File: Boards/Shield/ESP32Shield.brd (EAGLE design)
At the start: 58.4 x 25.4 mm, 26 parts, among them Q1 220mA/50V/3.5Ω, U1 5V

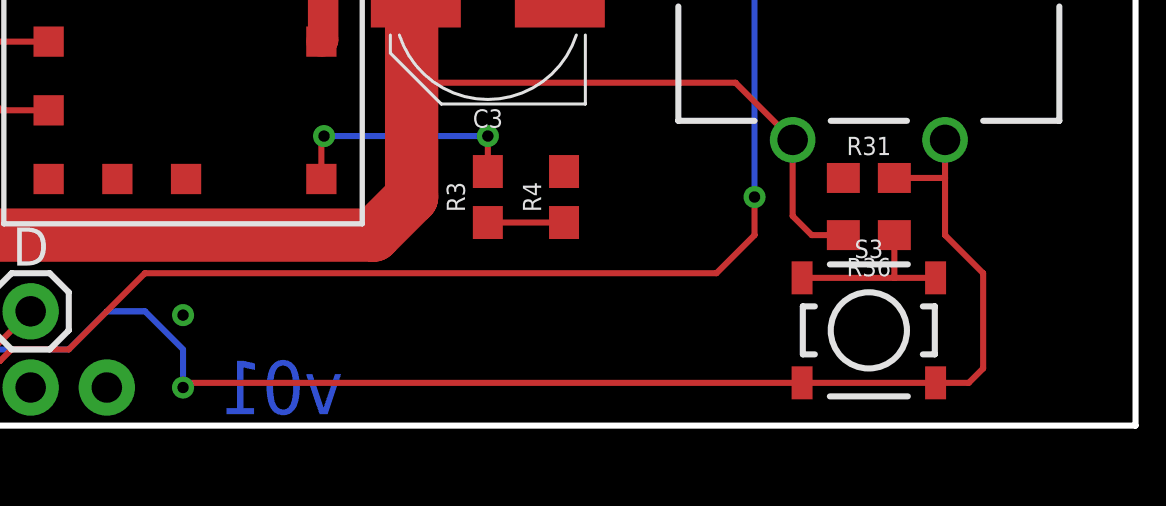
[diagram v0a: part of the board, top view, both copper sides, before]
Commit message: adding new pushbutton
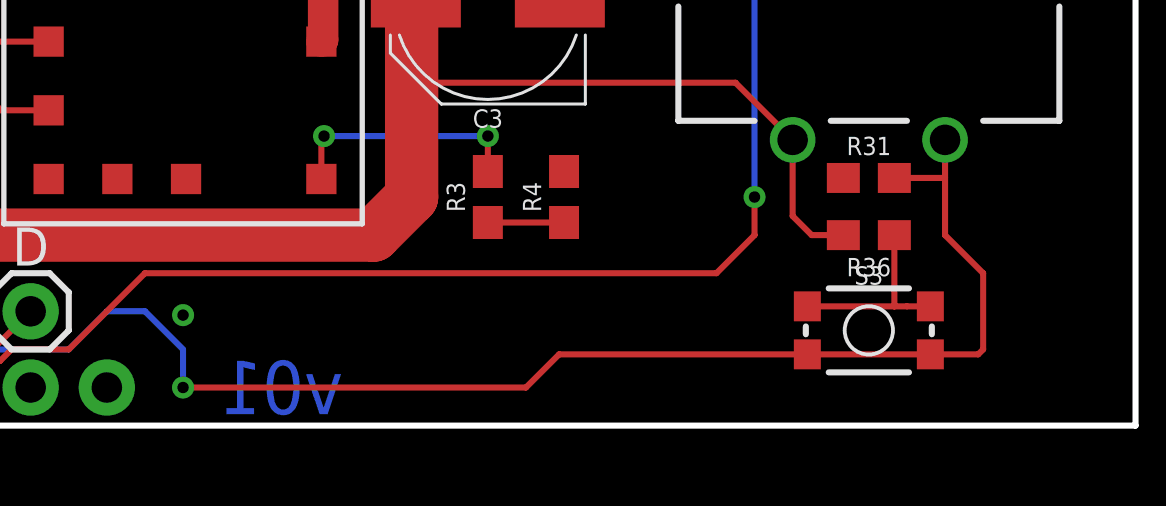
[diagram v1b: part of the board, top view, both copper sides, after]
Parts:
- S3: value MOMENTARY-SWITCH-SPST-SMD-4.5MM -> MOMENTARY-SWITCH-SPST-SMD-4.6X2.8MM; device SparkFun-Switches:TACTILE_SWITCH_SMD_4.5MM -> SparkFun-Switches:TACTILE_SWITCH_SMD_4.6X2.8MM
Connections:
- net BTN: now also S3.1; no longer S3.3
- net N$17: now also S3.3; no longer S3.1
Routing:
- net N$17: track 5.88 -> 6.48 mm
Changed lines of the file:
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@@
 <attribute name="SF_SKU" value="COM-09117" x="49.53" y="13.97" size="1.778" layer="27" rot="R90" display="off"/>
 </element>
-<element name="S3" library="SparkFun-Switches" package="TACTILE_SWITCH_SMD_4.5MM" value="MOMENTARY-SWITCH-SPST-SMD-4.5MM" x="49.53" y="0.635">
-<attribute name="PROD_ID" value="SWCH-09213" x="49.53" y="0.635" size="1.778" layer="27" display="off"/>
+<element name="S3" library="SparkFun-Switches" package="TACTILE_SWITCH_SMD_4.6X2.8MM" value="MOMENTARY-SWITCH-SPST-SMD-4.6X2.8MM" x="49.53" y="0.635">
+<attribute name="PROD_ID" value="SWCH-13065" x="49.53" y="0.635" size="1.778" layer="27" display="off"/>
 </element>
 <element name="U$2" library="SparkFun-IC-Power" package="DC-DC_CONVERTER" value="DC-DC_CONVERTER" x="26.67" y="10.16"/>
@@
 <contactref element="R31" pad="2"/>
 <contactref element="S3" pad="2"/>
-<contactref element="S3" pad="3"/>
+<contactref element="S3" pad="1"/>
 <contactref element="S1" pad="SW-"/>
 <wire x1="52.07" y1="6.985" x2="52.07" y2="5.715" width="0.2032" layer="1"/>
 <wire x1="52.07" y1="5.715" x2="52.07" y2="3.81" width="0.2032" layer="1"/>
 <wire x1="52.07" y1="3.81" x2="53.34" y2="2.54" width="0.2032" layer="1"/>
-<wire x1="53.34" y1="2.54" x2="53.34" y2="-0.635" width="0.2032" layer="1"/>
-<wire x1="53.34" y1="-0.635" x2="52.86" y2="-1.115" width="0.2032" layer="1"/>
-<wire x1="52.86" y1="-1.115" x2="51.755" y2="-1.115" width="0.2032" layer="1"/>
-<wire x1="51.755" y1="-1.115" x2="47.305" y2="-1.115" width="0.2032" layer="1"/>
+<wire x1="51.58" y1="-0.165" x2="47.48" y2="-0.165" width="0.2032" layer="1"/>
 <wire x1="50.38" y1="5.715" x2="52.07" y2="5.715" width="0.2032" layer="1"/>
 <via x="26.67" y="-1.27" extent="1-16" drill="0.381"/>
@@
 <wire x1="22.86" y1="0" x2="5.08" y2="0" width="0.2032" layer="16"/>
 <wire x1="26.67" y1="-1.27" x2="26.825" y2="-1.115" width="0.2032" layer="1"/>
-<wire x1="26.825" y1="-1.115" x2="47.305" y2="-1.115" width="0.2032" layer="1"/>
 <contactref element="J6" pad="2"/>
 <wire x1="3.81" y1="-1.27" x2="5.08" y2="0" width="0.2032" layer="16"/>
+<wire x1="53.34" y1="2.54" x2="53.34" y2="0" width="0.2032" layer="1"/>
+<wire x1="53.34" y1="0" x2="53.175" y2="-0.165" width="0.2032" layer="1"/>
+<wire x1="53.175" y1="-0.165" x2="51.58" y2="-0.165" width="0.2032" layer="1"/>
+<wire x1="47.48" y1="-0.165" x2="39.205" y2="-0.165" width="0.2032" layer="1"/>
+<wire x1="39.205" y1="-0.165" x2="38.1" y2="-1.27" width="0.2032" layer="1"/>
+<wire x1="38.1" y1="-1.27" x2="26.67" y2="-1.27" width="0.2032" layer="1"/>
 </signal>
 <signal name="N$17">
 <contactref element="R36" pad="1"/>
-<contactref element="S3" pad="1"/>
+<contactref element="S3" pad="3"/>
 <contactref element="S3" pad="4"/>
-<wire x1="51.755" y1="2.385" x2="50.38" y2="2.385" width="0.2032" layer="1"/>
-<wire x1="50.38" y1="2.385" x2="47.305" y2="2.385" width="0.2032" layer="1"/>
-<wire x1="50.38" y1="3.81" x2="50.38" y2="2.385" width="0.2032" layer="1"/>
+<wire x1="50.38" y1="3.81" x2="50.38" y2="1.435" width="0.2032" layer="1"/>
+<wire x1="51.58" y1="1.435" x2="50.8" y2="1.435" width="0.2032" layer="1"/>
+<wire x1="50.38" y1="1.435" x2="47.48" y2="1.435" width="0.2032" layer="1"/>
+<wire x1="50.38" y1="1.435" x2="50.8" y2="1.435" width="0.2032" layer="1"/>
 </signal>
 <signal name="VBATT">

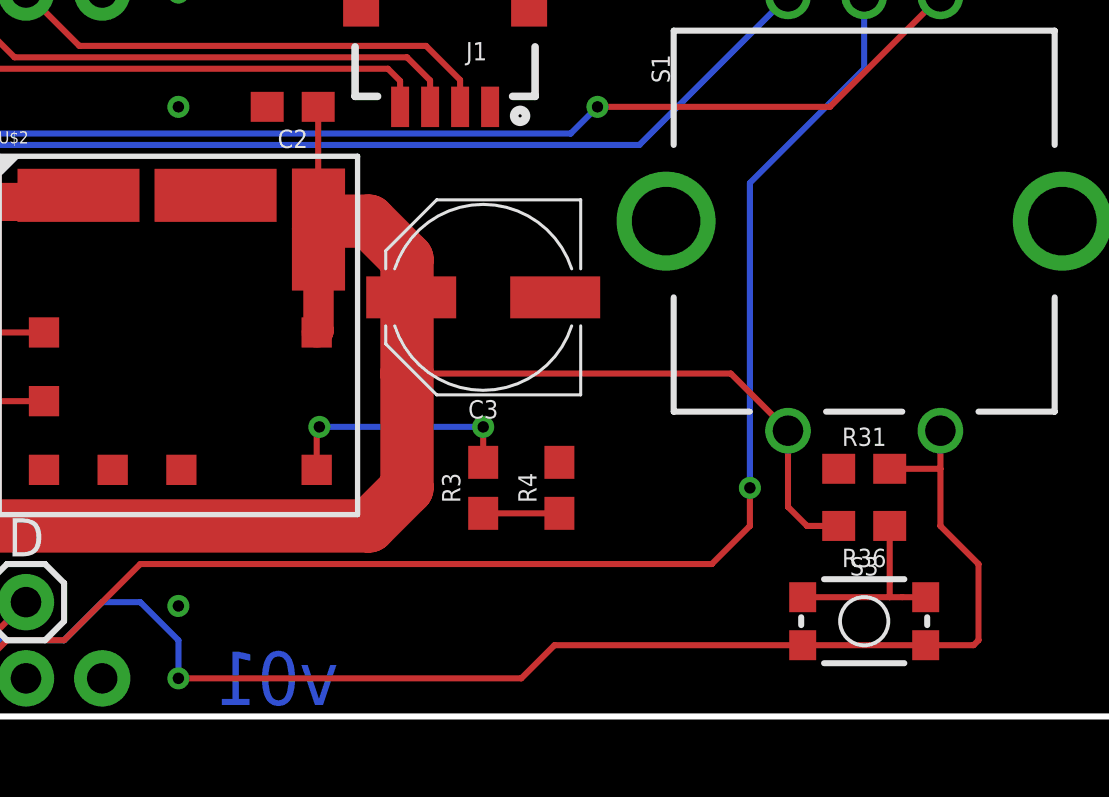
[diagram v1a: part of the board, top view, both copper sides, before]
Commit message: updated resistors, silk
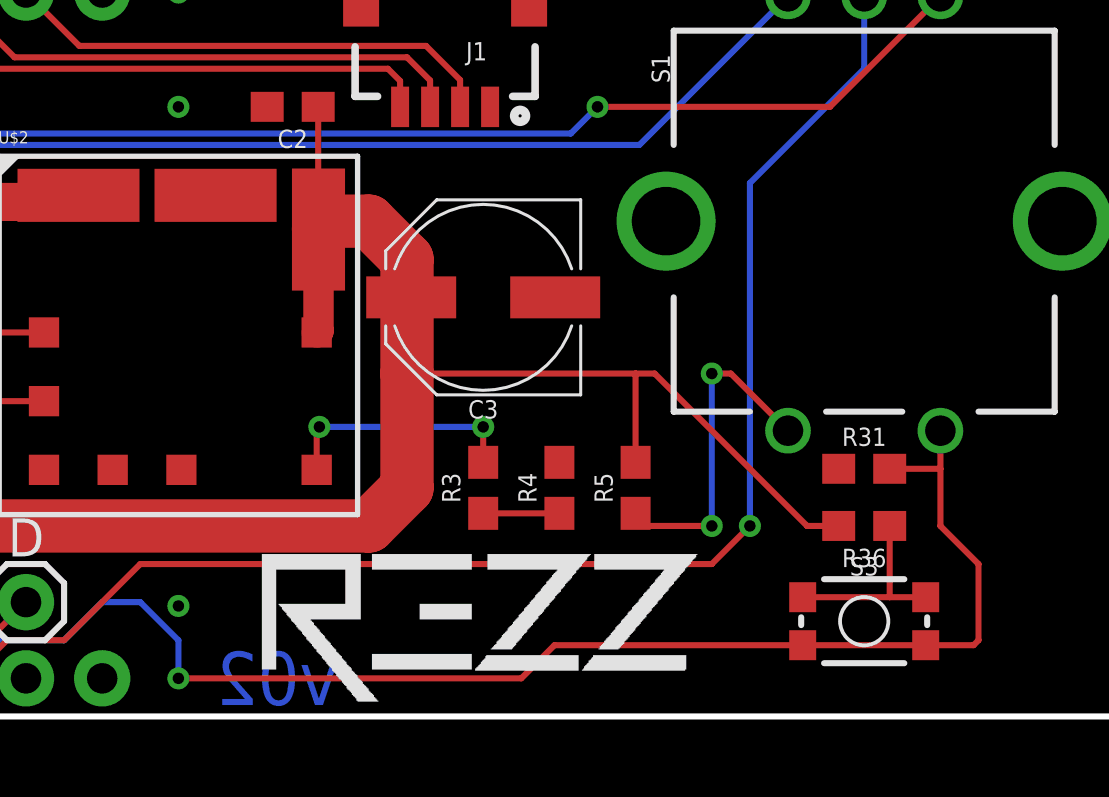
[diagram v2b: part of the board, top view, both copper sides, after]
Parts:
- added R5: 43k, SparkFun-Resistors:0603
- added U$1, U$4: (no value), SWbaDNC#jpg (1):SWBADNC#JPG
- added U$3: (no value), fb847930393b0f397fc054233c2d7cc6f23d0e39#jpg (1):FB847930393B0F397FC054233C2D7CC6F23D0E39#JPG
- R36: value 20k -> 100k
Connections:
- new net N$6: R5.1, S1.SW+
- net 5V: now also R5.2; no longer S1.SW+
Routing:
- net N$6: track 0.00 -> 11.1 mm, vias 0 -> 2
- net 5V: track 98.7 -> 100.1 mm
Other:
- board text added: "v02"
- board text removed: "REZZ Glasses Control"
- board text removed: "v01"

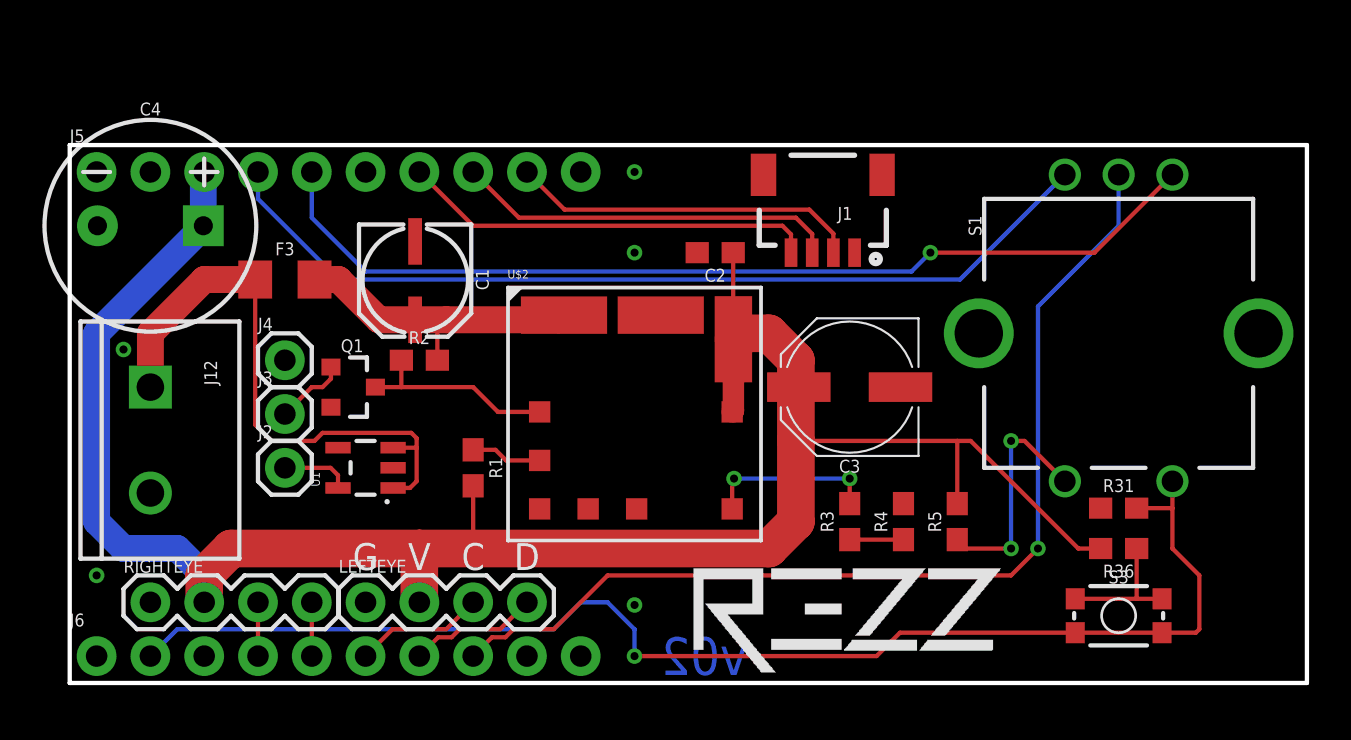
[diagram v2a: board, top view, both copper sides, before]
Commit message: Updating interrupts, power structure
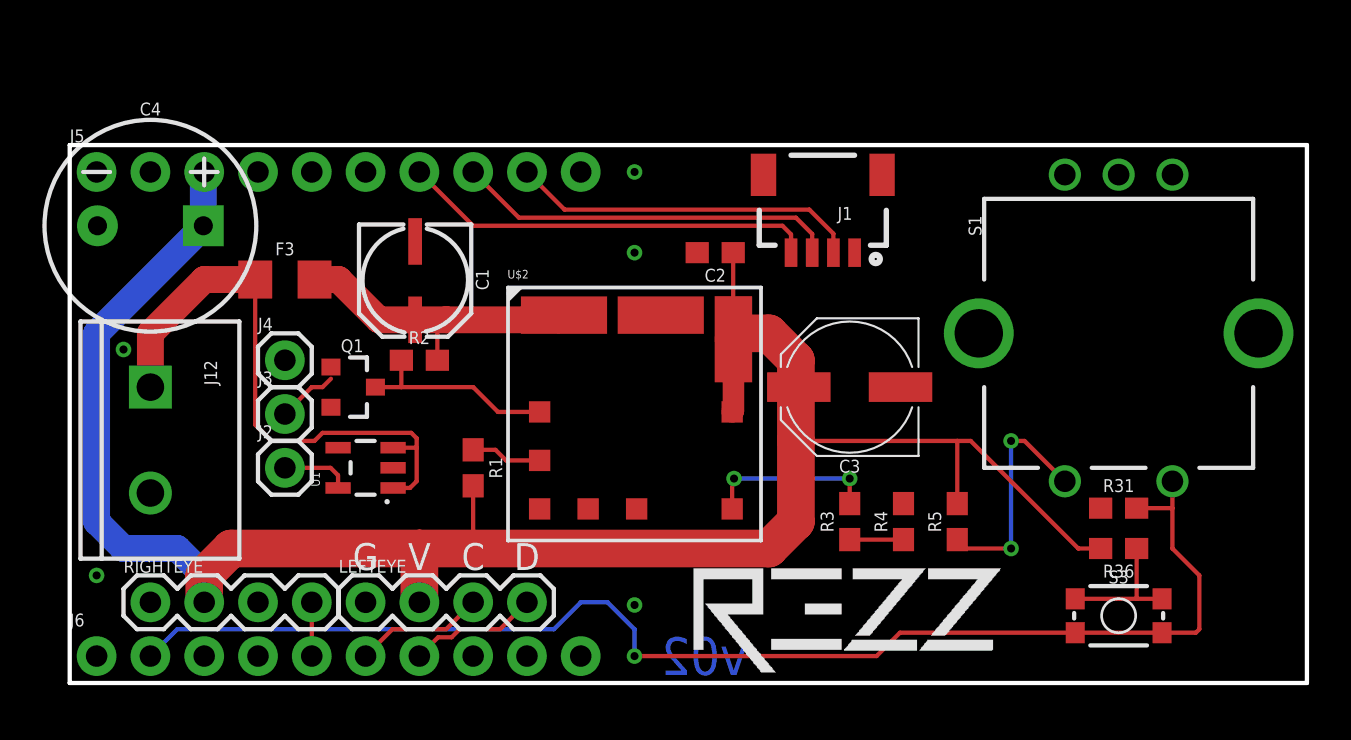
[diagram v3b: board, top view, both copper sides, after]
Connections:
- removed net CR: J6.4, RIGHTEYE.3
- removed net ENC-C: J6.8, S1.C
- new net BTNINT: J6.1
- net CL: now also RIGHTEYE.3
- net ENC-A: now also J6.8; no longer J5.5
- net ENC-B: now also J6.4; no longer J5.4
- net GND: now also S1.C
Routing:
- net ENC-C: track 48.0 -> 0.00 mm, vias 1 -> 0
- net ENC-A: track 45.7 -> 0.00 mm, vias 1 -> 0
- net ENC-B: track 43.0 -> 0.00 mm
- net CR: track 2.54 -> 0.00 mm
- net N$1: track 3.42 -> 2.87 mm
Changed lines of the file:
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@@
 <via x="26.67" y="21.59" extent="1-16" drill="0.381"/>
 <via x="26.67" y="17.78" extent="1-16" drill="0.381"/>
+<contactref element="S1" pad="C"/>
 </signal>
 <signal name="BTN">
@@
 <contactref element="J6" pad="6"/>
 <wire x1="13.97" y1="-1.27" x2="15.24" y2="0" width="0.2032" layer="1"/>
+<contactref element="RIGHTEYE" pad="3"/>
+<wire x1="8.89" y1="1.27" x2="13.97" y2="-1.27" width="0" layer="19" extent="1-1"/>
 </signal>
 <signal name="DR">
@@
 <wire x1="11.43" y1="-1.27" x2="11.43" y2="1.27" width="0.2032" layer="1"/>
 </signal>
-<signal name="CR">
-<contactref element="RIGHTEYE" pad="3"/>
-<contactref element="J6" pad="4"/>
-<wire x1="8.89" y1="1.27" x2="8.89" y2="-1.27" width="0.2032" layer="1"/>
-</signal>
 <signal name="ENC-A">
 <contactref element="S1" pad="A"/>
-<contactref element="J5" pad="5"/>
-<wire x1="52.07" y1="21.463" x2="48.387" y2="17.78" width="0.2032" layer="1"/>
-<wire x1="48.387" y1="17.78" x2="40.64" y2="17.78" width="0.2032" layer="1"/>
-<via x="40.64" y="17.78" extent="1-16" drill="0.381"/>
-<wire x1="40.64" y1="17.78" x2="39.751" y2="16.891" width="0.2032" layer="16"/>
-<wire x1="39.751" y1="16.891" x2="13.97" y2="16.891" width="0.2032" layer="16"/>
-<wire x1="13.97" y1="16.891" x2="11.43" y2="19.431" width="0.2032" layer="16"/>
-<wire x1="11.43" y1="19.431" x2="11.43" y2="21.59" width="0.2032" layer="16"/>
-</signal>
-<signal name="ENC-C">
-<contactref element="S1" pad="C"/>
-<wire x1="19.939" y1="-0.381" x2="20.574" y2="-0.381" width="0.2032" layer="1"/>
-<wire x1="20.574" y1="-0.381" x2="20.955" y2="0" width="0.2032" layer="1"/>
-<wire x1="20.955" y1="0" x2="22.86" y2="0" width="0.2032" layer="1"/>
-<wire x1="22.86" y1="0" x2="25.4" y2="2.54" width="0.2032" layer="1"/>
-<wire x1="25.4" y1="2.54" x2="44.45" y2="2.54" width="0.2032" layer="1"/>
-<wire x1="44.45" y1="2.54" x2="45.72" y2="3.81" width="0.2032" layer="1"/>
-<via x="45.72" y="3.81" extent="1-16" drill="0.381"/>
-<wire x1="45.72" y1="3.81" x2="45.72" y2="15.24" width="0.2032" layer="16"/>
-<wire x1="45.72" y1="15.24" x2="49.53" y2="19.05" width="0.2032" layer="16"/>
-<wire x1="49.53" y1="19.05" x2="49.53" y2="21.463" width="0.2032" layer="16"/>
 <contactref element="J6" pad="8"/>
-<wire x1="19.05" y1="-1.27" x2="19.939" y2="-0.381" width="0.2032" layer="1"/>
+<wire x1="19.05" y1="-1.27" x2="52.07" y2="21.463" width="0" layer="19" extent="1-1"/>
 </signal>
 <signal name="ENC-B">
 <contactref element="S1" pad="B"/>
-<contactref element="J5" pad="4"/>
-<wire x1="46.99" y1="21.463" x2="42.037" y2="16.51" width="0.2032" layer="16"/>
-<wire x1="42.037" y1="16.51" x2="12.7" y2="16.51" width="0.2032" layer="16"/>
-<wire x1="12.7" y1="16.51" x2="8.89" y2="20.32" width="0.2032" layer="16"/>
-<wire x1="8.89" y1="20.32" x2="8.89" y2="21.59" width="0.2032" layer="16"/>
+<contactref element="J6" pad="4"/>
+<wire x1="8.89" y1="-1.27" x2="46.99" y2="21.463" width="0" layer="19" extent="1-1"/>
 </signal>
 <signal name="N$1">
@@
 <wire x1="11.43" y1="11.43" x2="11.938" y2="11.43" width="0.2032" layer="1"/>
 <wire x1="11.938" y1="11.43" x2="12.335" y2="11.827" width="0.2032" layer="1"/>
-<wire x1="12.335" y1="11.827" x2="12.335" y2="12.38" width="0.2032" layer="1"/>
+<wire x1="12.335" y1="11.827" x2="12.335" y2="12.38" width="0" layer="19" extent="1-16"/>
 </signal>
 <signal name="N$6">
@@
 <wire x1="45.085" y1="8.89" x2="46.99" y2="6.985" width="0.2032" layer="1"/>
 </signal>
+<signal name="BTNINT">
+<contactref element="J6" pad="1"/>
+</signal>
 </signals>
